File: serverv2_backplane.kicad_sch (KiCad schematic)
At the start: 49 parts, among them J1 Conn_02x12_Counter_Clockwise, U1 RTL9210B-CG, U2 W25Q128JVSIQTR, U3 ETA3521FSG_C22362743, X1 X322525MOB4SI

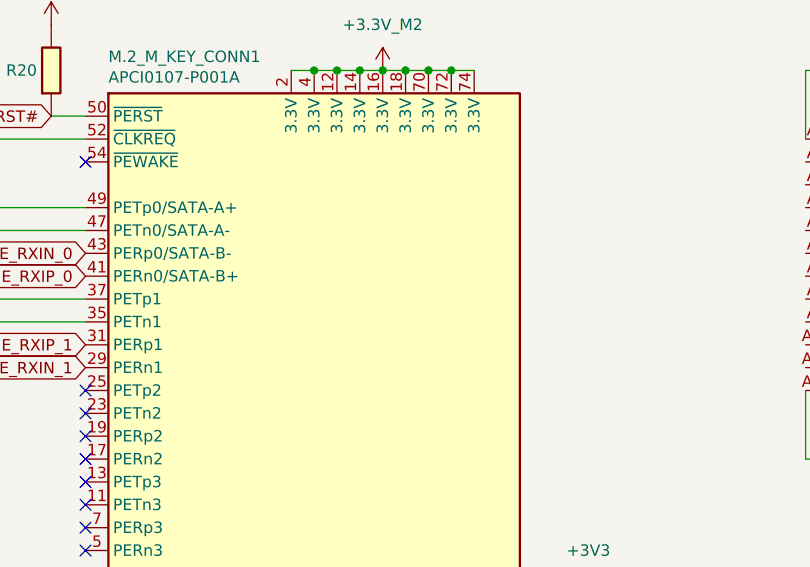
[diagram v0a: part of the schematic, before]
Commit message: Created first draft of RP2350B circuit and added 0.85in display connectors
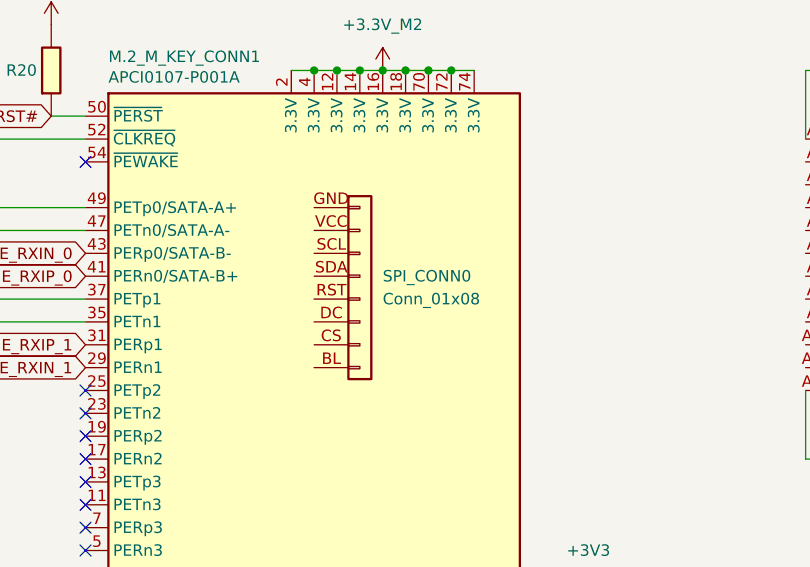
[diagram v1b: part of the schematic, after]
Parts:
- added SPI_CONN0: Conn_01x08, symbol Connector_Generic:Conn_01x08
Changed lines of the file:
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@@
+		)
+	)
+	(symbol
+		(lib_id "Connector_Generic:Conn_01x08")
+		(at 85.09 45.72 0)
+		(unit 1)
+		(body_style 1)
+		(exclude_from_sim no)
+		(in_bom yes)
+		(on_board yes)
+		(in_pos_files yes)
+		(dnp no)
+		(fields_autoplaced yes)
+		(property "Reference" "SPI_CONN0"
+			(at 87.63 45.7199 0)
+			(show_name no)
+			(do_not_autoplace no)
+			(effects
+				(font
+					(size 1.27 1.27)
+				)
+				(justify left)
+			)
+		)
+		(property "Value" "Conn_01x08"
+			(at 87.63 48.2599 0)
+			(show_name no)
+			(do_not_autoplace no)
+			(effects
+				(font
+					(size 1.27 1.27)
+				)
+				(justify left)
+			)
+		)
+		(property "Footprint" ""
+			(at 85.09 45.72 0)
+			(hide yes)
+			(show_name no)
+			(do_not_autoplace no)
+			(effects
+				(font
+					(size 1.27 1.27)
+				)
+			)
+		)
+		(property "Datasheet" ""
+			(at 85.09 45.72 0)
+			(hide yes)
+			(show_name no)
+			(do_not_autoplace no)
+			(effects
+				(font
+					(size 1.27 1.27)
+				)
+			)
+		)
+		(property "Description" "Generic connector, single row, 01x08, script generated (kicad-library-utils/schlib/autogen/connector/)"
+			(at 85.09 45.72 0)
+			(hide yes)
+			(show_name no)
+			(do_not_autoplace no)
+			(effects
+				(font
+					(size 1.27 1.27)
+				)
+			)
+		)
+		(pin "CS"
+		)
+		(pin "SCL"
+		)
+		(pin "SDA"
+		)
+		(pin "DC"
+		)
+		(pin "GND"
+		)
+		(pin "BL"
+		)
+		(pin "VCC"
+		)
+		(pin "RST"
+		)
+		(instances
+			(project "serverv2_backplane"
+				(path "/d38d6818-cf53-410d-afa3-a75a85b7c05a"
+					(reference "SPI_CONN0")
+					(unit 1)
+				)
+			)
 		)
 	)

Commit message: Changed to touchscreen LCD and added connectors for front breakout
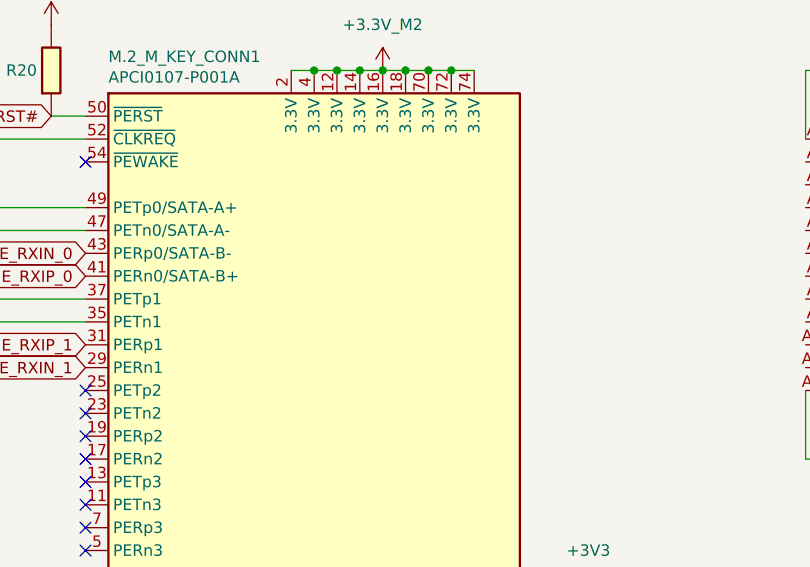
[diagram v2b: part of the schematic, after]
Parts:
- removed SPI_CONN0: Conn_01x08, symbol Connector_Generic:Conn_01x08
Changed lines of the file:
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@@
-		)
-	)
-	(symbol
-		(lib_id "Connector_Generic:Conn_01x08")
-		(at 85.09 45.72 0)
-		(unit 1)
-		(body_style 1)
-		(exclude_from_sim no)
-		(in_bom yes)
-		(on_board yes)
-		(in_pos_files yes)
-		(dnp no)
-		(fields_autoplaced yes)
-		(property "Reference" "SPI_CONN0"
-			(at 87.63 45.7199 0)
-			(show_name no)
-			(do_not_autoplace no)
-			(effects
-				(font
-					(size 1.27 1.27)
-				)
-				(justify left)
-			)
-		)
-		(property "Value" "Conn_01x08"
-			(at 87.63 48.2599 0)
-			(show_name no)
-			(do_not_autoplace no)
-			(effects
-				(font
-					(size 1.27 1.27)
-				)
-				(justify left)
-			)
-		)
-		(property "Footprint" ""
-			(at 85.09 45.72 0)
-			(hide yes)
-			(show_name no)
-			(do_not_autoplace no)
-			(effects
-				(font
-					(size 1.27 1.27)
-				)
-			)
-		)
-		(property "Datasheet" ""
-			(at 85.09 45.72 0)
-			(hide yes)
-			(show_name no)
-			(do_not_autoplace no)
-			(effects
-				(font
-					(size 1.27 1.27)
-				)
-			)
-		)
-		(property "Description" "Generic connector, single row, 01x08, script generated (kicad-library-utils/schlib/autogen/connector/)"
-			(at 85.09 45.72 0)
-			(hide yes)
-			(show_name no)
-			(do_not_autoplace no)
-			(effects
-				(font
-					(size 1.27 1.27)
-				)
-			)
-		)
-		(pin "CS"
-		)
-		(pin "SCL"
-		)
-		(pin "SDA"
-		)
-		(pin "DC"
-		)
-		(pin "GND"
-		)
-		(pin "BL"
-		)
-		(pin "VCC"
-		)
-		(pin "RST"
-		)
-		(instances
-			(project "serverv2_backplane"
-				(path "/d38d6818-cf53-410d-afa3-a75a85b7c05a"
-					(reference "SPI_CONN0")
-					(unit 1)
-				)
-			)
 		)
 	)
